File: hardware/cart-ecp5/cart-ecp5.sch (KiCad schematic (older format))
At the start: 16 parts, among them U3 FAN53541

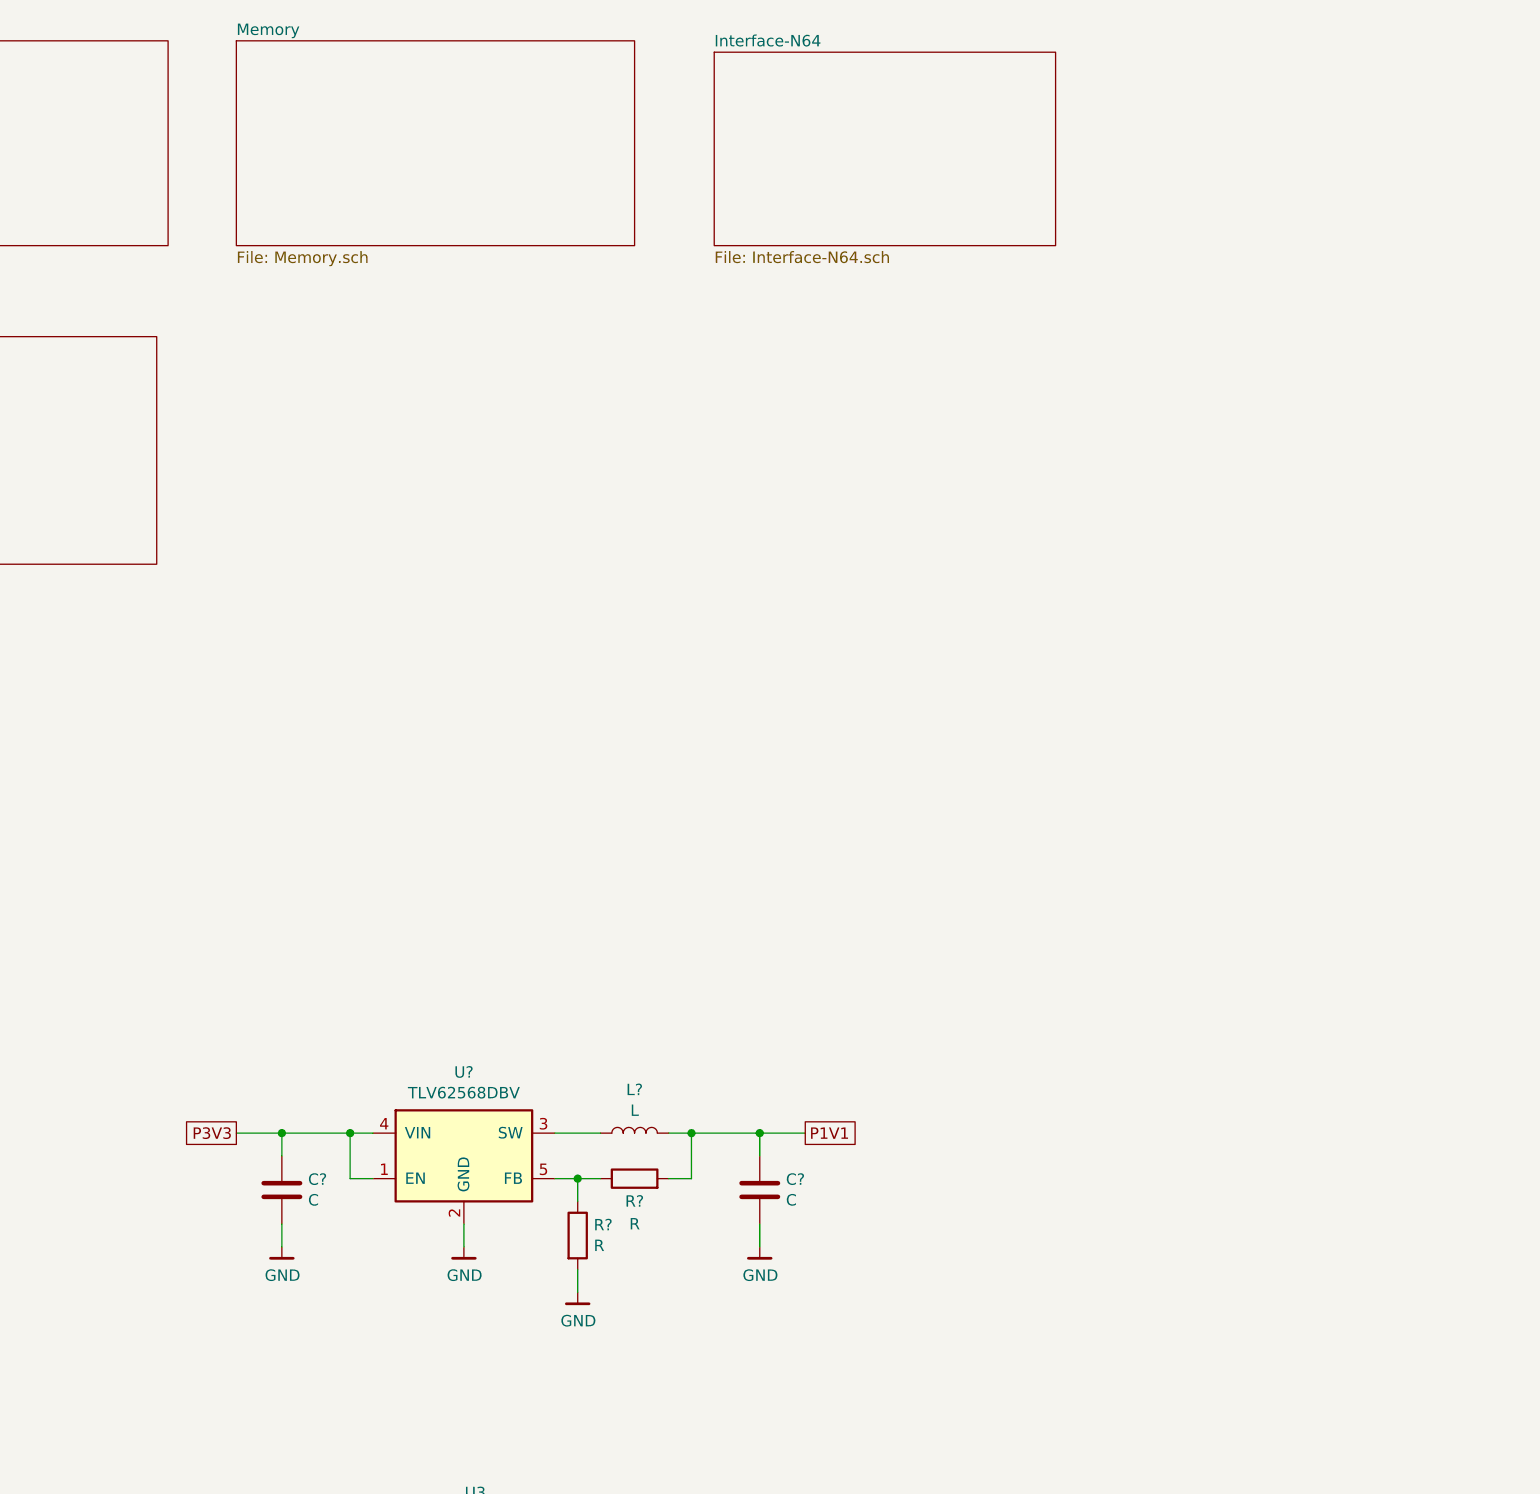
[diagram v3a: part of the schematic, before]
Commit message: Add power muxing and regulators for P3V3, P2V5, and P1V1 rails
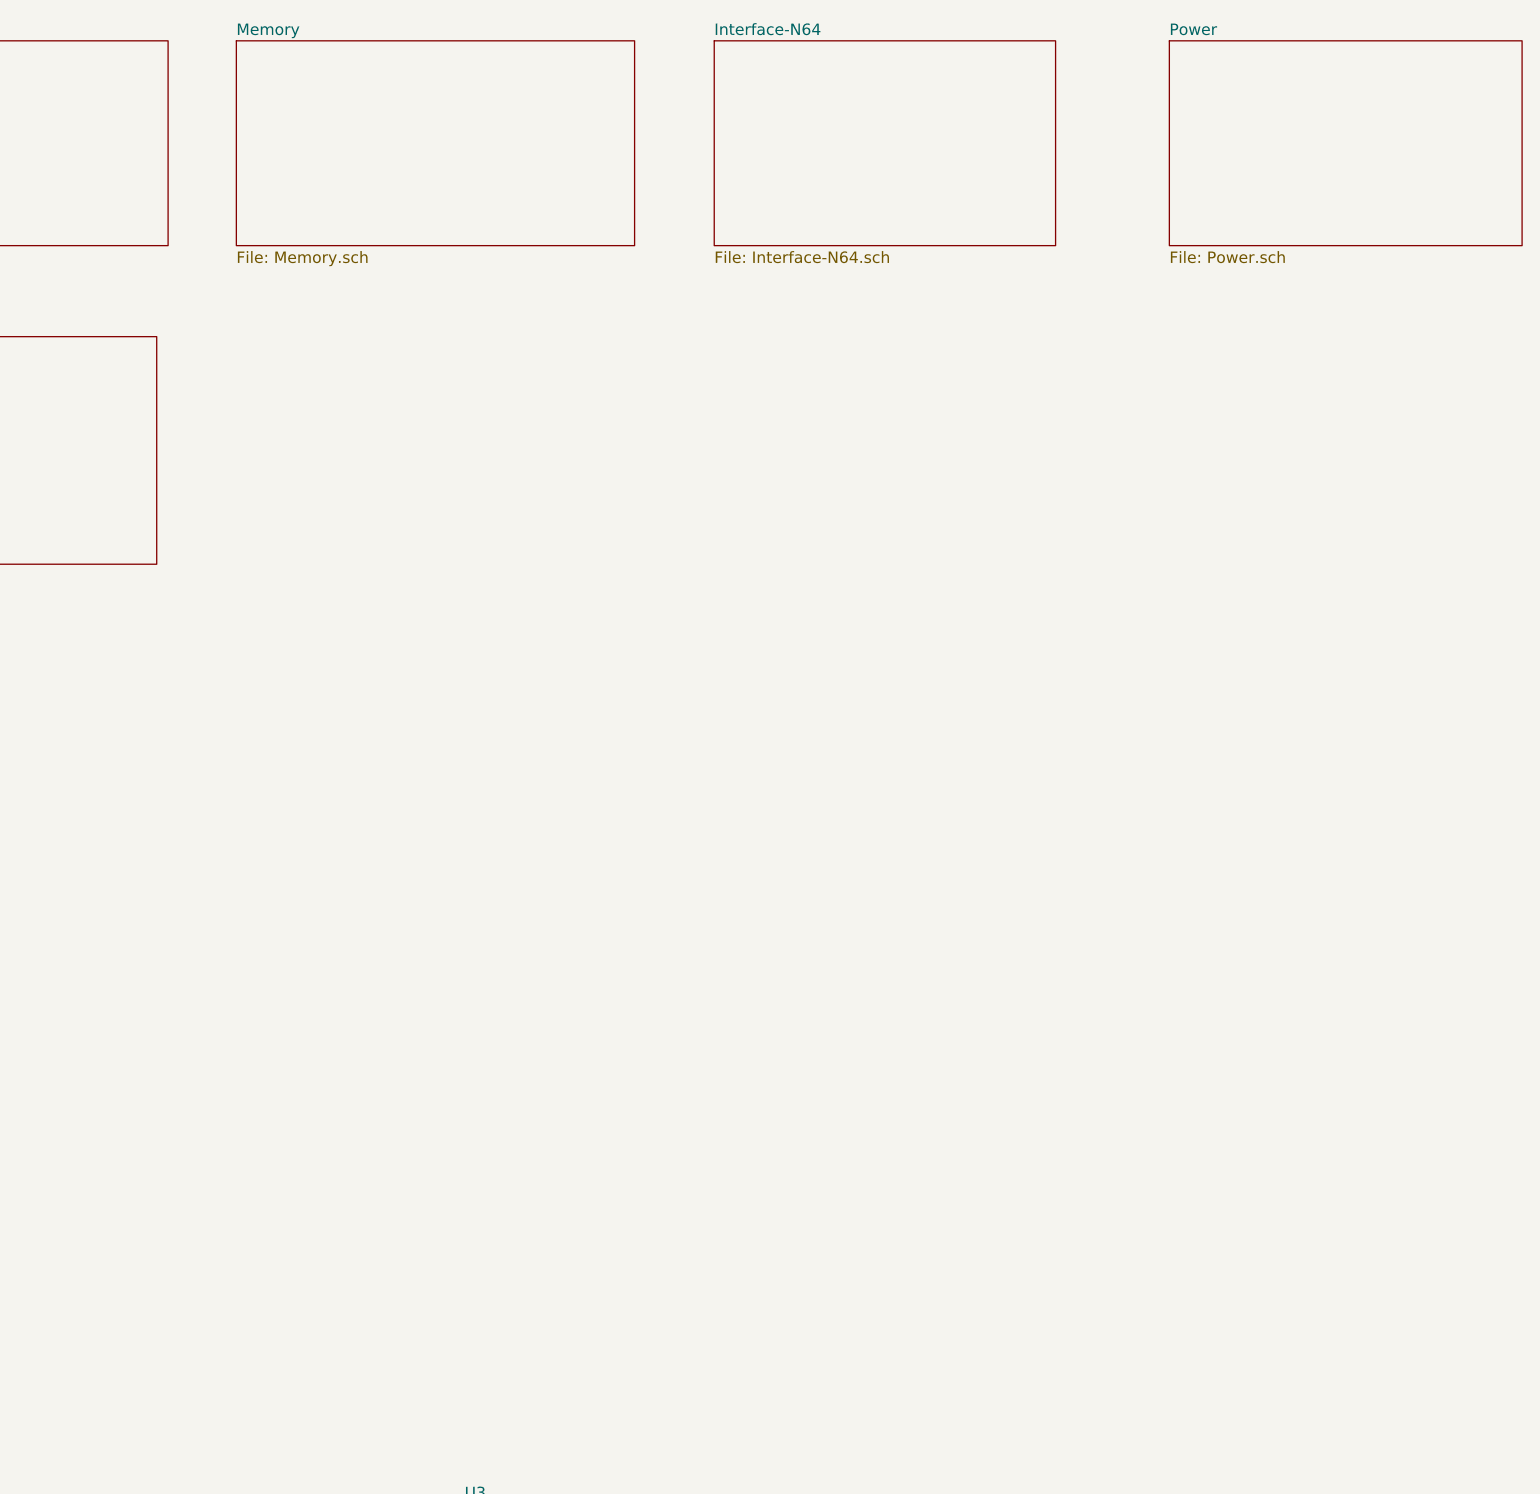
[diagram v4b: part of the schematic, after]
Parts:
- removed C? (x2): C, symbol Device:C
- removed L?: L, symbol Device:L
- removed R? (x2): R, symbol Device:R
- removed U?: TLV62568DBV, Package_TO_SOT_SMD:SOT-23-5, symbol ng_regulator:TLV62568DBV
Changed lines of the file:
@@
 $Descr A3 16535 11693
 encoding utf-8
-Sheet 1 5
+Sheet 1 6
 Title ""
 Date ""
@@
 $EndSheet
 $Sheet
-S 6000 1500 1500 850
+S 6000 1450 1500 900
 U 5F43B1FD
 F0 "Interface-N64" 50
 F1 "Interface-N64.sch" 50
 $EndSheet
-$Comp
-L ng_regulator:TLV62568DBV U?
-U 1 1 5F448D14
-P 4900 6300
-F 0 "U?" H 4900 6617 50  0000 C CNN
-F 1 "TLV62568DBV" H 4900 6526 50  0000 C CNN
-F 2 "Package_TO_SOT_SMD:SOT-23-5" H 4900 5850 50  0001 C CNN
-F 3 "https://www.ti.com/lit/ds/symlink/tlv62568.pdf" H 4900 6250 50  0001 C CNN
-	1    4900 6300
-	1    0    0    -1
-$EndComp
-$Comp
-L Device:L L?
-U 1 1 5F44F41D
-P 5650 6250
-F 0 "L?" V 5840 6250 50  0000 C CNN
-F 1 "L" V 5749 6250 50  0000 C CNN
-F 2 "" H 5650 6250 50  0001 C CNN
-F 3 "~" H 5650 6250 50  0001 C CNN
-	1    5650 6250
-	0    -1   -1   0
-$EndComp
-$Comp
-L Device:R R?
-U 1 1 5F45018E
-P 5400 6700
-F 0 "R?" H 5470 6746 50  0000 L CNN
-F 1 "R" H 5470 6655 50  0000 L CNN
-F 2 "" V 5330 6700 50  0001 C CNN
-F 3 "~" H 5400 6700 50  0001 C CNN
-	1    5400 6700
-	1    0    0    -1
-$EndComp
-$Comp
-L Device:R R?
-U 1 1 5F4511AF
-P 5650 6450
-F 0 "R?" V 5550 6450 50  0000 C CNN
-F 1 "R" V 5450 6450 50  0000 C CNN
-F 2 "" V 5580 6450 50  0001 C CNN
-F 3 "~" H 5650 6450 50  0001 C CNN
-	1    5650 6450
-	0    -1   -1   0
-$EndComp
-Wire Wire Line
-	5800 6450 5900 6450
-Wire Wire Line
-	5900 6450 5900 6250
-Wire Wire Line
-	5900 6250 5800 6250
-Wire Wire Line
-	5500 6250 5300 6250
-Wire Wire Line
-	5300 6450 5400 6450
-Wire Wire Line
-	5400 6550 5400 6450
-$Comp
-L Device:C C?
-U 1 1 5F4599C0
-P 6200 6500
-F 0 "C?" H 6315 6546 50  0000 L CNN
-F 1 "C" H 6315 6455 50  0000 L CNN
-F 2 "" H 6238 6350 50  0001 C CNN
-F 3 "~" H 6200 6500 50  0001 C CNN
-	1    6200 6500
-	1    0    0    -1
-$EndComp
-Wire Wire Line
-	5900 6250 6200 6250
-Wire Wire Line
-	6200 6250 6200 6350
-Connection ~ 5900 6250
-Wire Wire Line
-	6200 6650 6200 6750
-Wire Wire Line
-	5400 6850 5400 6950
-Wire Wire Line
-	4900 6650 4900 6750
-$Comp
-L Device:C C?
-U 1 1 5F46367C
-P 4100 6500
-F 0 "C?" H 4215 6546 50  0000 L CNN
-F 1 "C" H 4215 6455 50  0000 L CNN
-F 2 "" H 4138 6350 50  0001 C CNN
-F 3 "~" H 4100 6500 50  0001 C CNN
-	1    4100 6500
-	1    0    0    -1
-$EndComp
-Wire Wire Line
-	4100 6250 4100 6350
-Wire Wire Line
-	4100 6650 4100 6750
-Wire Wire Line
-	4500 6450 4400 6450
-Wire Wire Line
-	4400 6450 4400 6250
-Wire Wire Line
-	4400 6250 4500 6250
-Wire Wire Line
-	4100 6250 4400 6250
-Connection ~ 4400 6250
-Wire Wire Line
-	4100 6250 3900 6250
-Connection ~ 4100 6250
-$Comp
-L ng_power:GND #PWR?
-U 1 1 5F46CFC1
-P 4900 6750
-F 0 "#PWR?" H 4900 6500 50  0001 C CNN
-F 1 "GND" H 4903 6624 50  0000 C CNN
-F 2 "" H 4800 6400 50  0001 C CNN
-F 3 "" H 4900 6750 50  0001 C CNN
-	1    4900 6750
-	1    0    0    -1
-$EndComp
-$Comp
-L ng_power:GND #PWR?
-U 1 1 5F46D00C
-P 4100 6750
-F 0 "#PWR?" H 4100 6500 50  0001 C CNN
-F 1 "GND" H 4103 6624 50  0000 C CNN
-F 2 "" H 4000 6400 50  0001 C CNN
-F 3 "" H 4100 6750 50  0001 C CNN
-	1    4100 6750
-	1    0    0    -1
-$EndComp
-$Comp
-L ng_power:GND #PWR?
-U 1 1 5F46D557
-P 6200 6750
-F 0 "#PWR?" H 6200 6500 50  0001 C CNN
-F 1 "GND" H 6203 6624 50  0000 C CNN
-F 2 "" H 6100 6400 50  0001 C CNN
-F 3 "" H 6200 6750 50  0001 C CNN
-	1    6200 6750
-	1    0    0    -1
-$EndComp
-$Comp
-L ng_power:GND #PWR?
-U 1 1 5F46DB3A
-P 5400 6950
-F 0 "#PWR?" H 5400 6700 50  0001 C CNN
-F 1 "GND" H 5403 6824 50  0000 C CNN
-F 2 "" H 5300 6600 50  0001 C CNN
-F 3 "" H 5400 6950 50  0001 C CNN
-	1    5400 6950
-	1    0    0    -1
-$EndComp
-Connection ~ 5400 6450
-Wire Wire Line
-	5400 6450 5500 6450
-Connection ~ 6200 6250
-Wire Wire Line
-	6200 6250 6400 6250
-Text GLabel 3900 6250 0    50   UnSpc ~ 0
-P3V3
-Text GLabel 6400 6250 2    50   UnSpc ~ 0
-P1V1
+$Sheet
+S 8000 1450 1550 900
+U 5F483803
+F0 "Power" 50
+F1 "Power.sch" 50
+$EndSheet
 $EndSCHEMATC
